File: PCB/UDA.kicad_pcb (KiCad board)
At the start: 2 copper layers, 48 x 48 mm, 36 parts, among them P1 CONN_01X05, U1 MCU-ATMEGA328P-AU(TQFP32), U2 MIC5205-3.3YM5

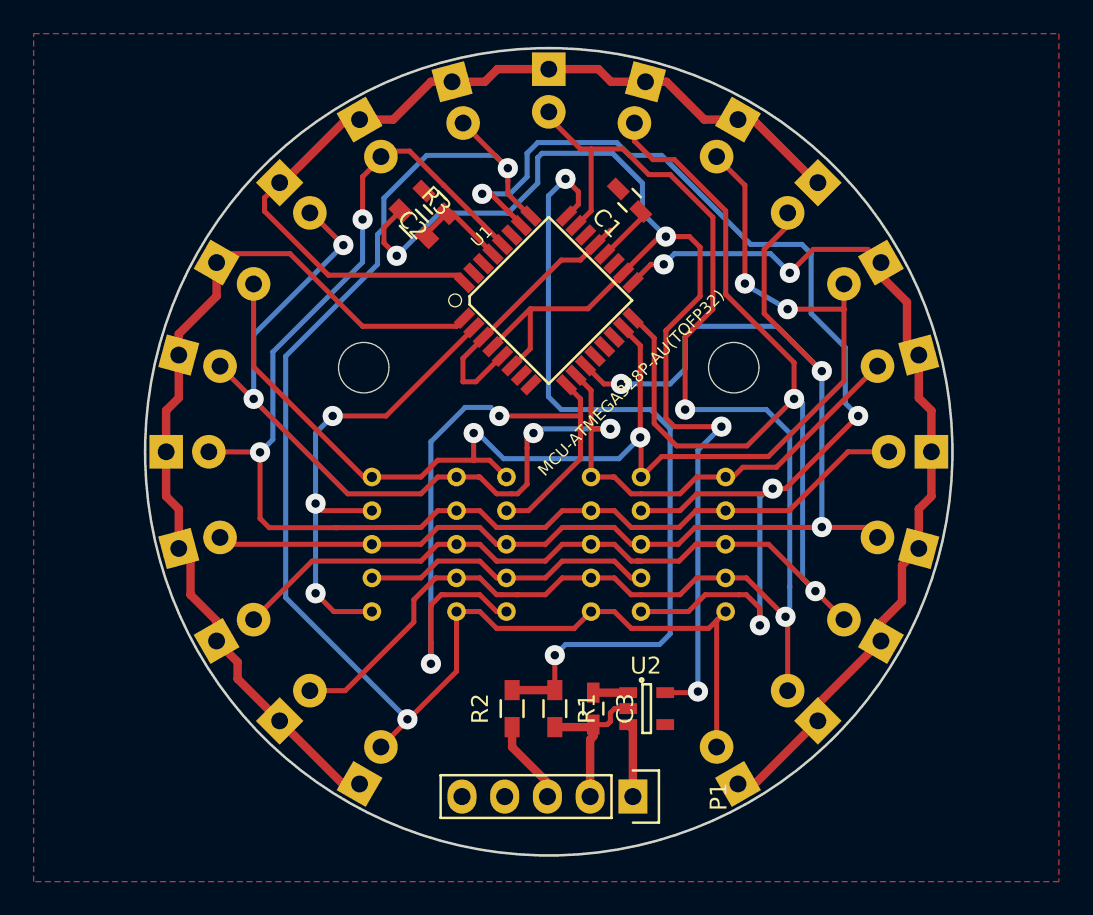
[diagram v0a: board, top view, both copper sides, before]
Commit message: - version finale restante a router
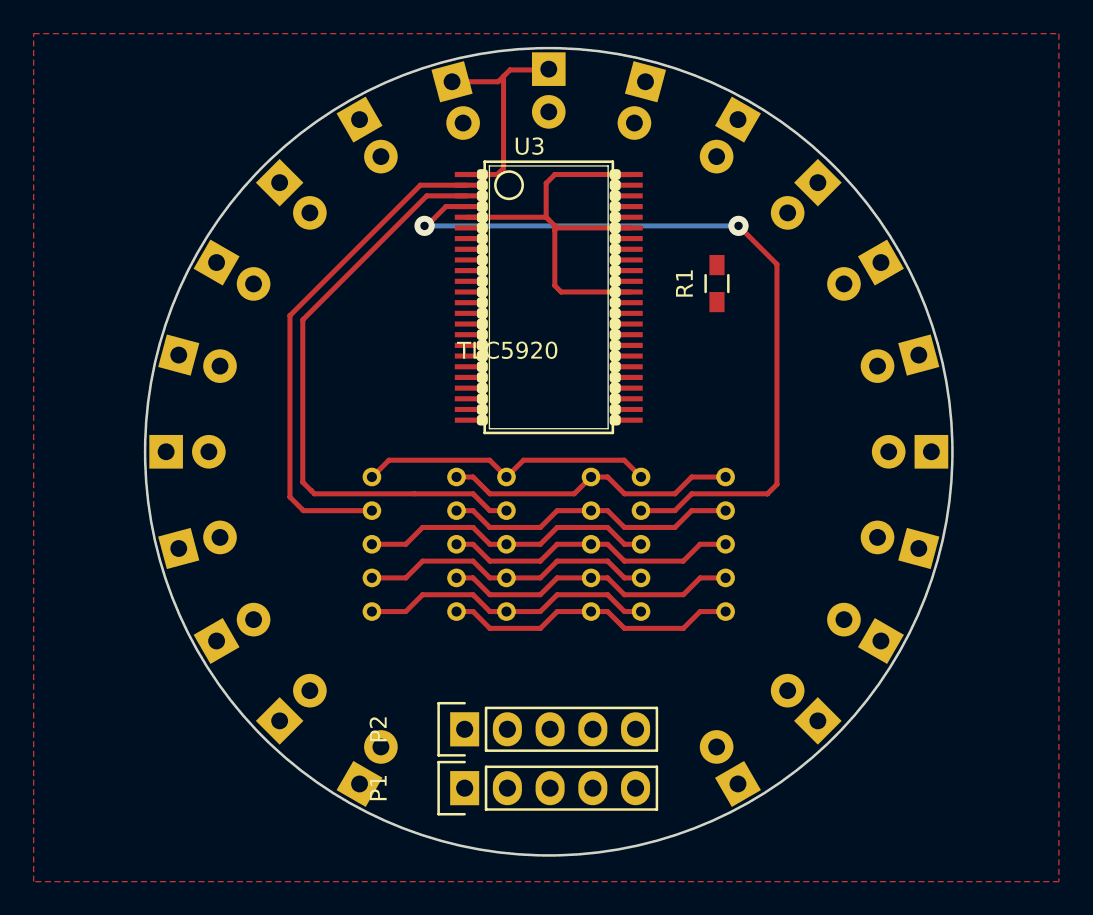
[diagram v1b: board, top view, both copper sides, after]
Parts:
- removed ? (x2): , Perçages:Trou_3mm
- removed C1, C2, C3: 0.1uF, condensateurs:C_0603_HandSoldering
- removed G***: LOGO, Logo:logo
- removed R2: 0.0, resistances:R_0603_HandSoldering
- removed R3: 10k, resistances:R_0603_HandSoldering
- removed U1: MCU-ATMEGA328P-AU(TQFP32), atmel:TQFP32-0.8-7X7MM
- removed U2: MIC5205-3.3YM5, resgulateurs:SOT-23-5
- added P2: CONN_01X05, Barrettes:Pin_Header_Straight_1x05, F.Cu at (81.0, 137.5)
- added U3: TLC5920, Drivers_Afficheurs:SSOP48DL, F.Cu at (86.0, 111.5)
- moved R1 27.0 mm to (96.0, 111.0), turned to 90 degrees
- moved P1 10.0 mm to (81.0, 141.0), turned to 90 degrees
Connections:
- D1 pad 1: COM4 -> COM3
- D1 pad 2: F -> S0
- D10 pad 1: COM5 -> COM3
- D10 pad 2: D -> S9
- D11 pad 1: COM5 -> COM3
- D11 pad 2: E -> S10
- D12 pad 1: COM5 -> COM4
- D12 pad 2: G -> S0
- D13 pad 1: COM5 -> COM4
- D13 pad 2: B -> S1
- D14 pad 1: COM6 -> COM4
- D14 pad 2: B -> S3
- D15 pad 1: COM5 -> COM4
- D15 pad 2: C -> S2
- D16 pad 1: COM6 -> COM4
- D16 pad 2: A -> S4
- D17 pad 1: COM6 -> COM4
- D17 pad 2: F -> S5
- D18 pad 1: COM6 -> COM4
- D18 pad 2: C -> S6
- D19 pad 1: COM6 -> COM4
- D19 pad 2: G -> S7
- D2 pad 1: COM4 -> COM3
- D2 pad 2: B -> S1
- D20 pad 1: COM6 -> COM4
- D20 pad 2: E -> S8
- D21 pad 1: COM6 -> COM4
- D21 pad 2: D -> S9
- D3 pad 1: COM4 -> COM3
- D3 pad 2: G -> S2
- D4 pad 1: COM4 -> COM3
- D4 pad 2: E -> S3
- D5 pad 1: COM4 -> COM3
- D5 pad 2: D -> S4
- D6 pad 1: COM4 -> COM3
- D6 pad 2: A -> S5
- D7 pad 1: COM4 -> COM3
- D7 pad 2: C -> S6
- D8 pad 1: COM5 -> COM3
- D8 pad 2: A -> S7
- D9 pad 1: COM5 -> COM3
- D9 pad 2: F -> S8
- LED1 pad 1: A -> S0
- LED1 pad 10: B -> S1
- LED1 pad 2: F -> S5
- LED1 pad 3: G -> S6
- LED1 pad 4: E -> S4
- LED1 pad 5: D -> S3
- LED1 pad 6: COM1 -> COM5
- LED1 pad 7: DP -> S7
- LED1 pad 8: C -> S2
- LED1 pad 9: COM1 -> COM0
- LED2 pad 1: A -> S0
- LED2 pad 10: B -> S1
- LED2 pad 2: F -> S5
- LED2 pad 3: G -> S6
- LED2 pad 4: E -> S4
- LED2 pad 5: D -> S3
- LED2 pad 6: COM2 -> COM5
- LED2 pad 7: DP -> S7
- LED2 pad 8: C -> S2
- LED2 pad 9: COM2 -> COM1
- LED3 pad 1: A -> S0
- LED3 pad 10: B -> S1
- LED3 pad 2: F -> S5
- LED3 pad 3: G -> S6
- LED3 pad 4: E -> S4
- LED3 pad 5: D -> S3
- LED3 pad 6: COM3 -> COM5
- LED3 pad 7: DP -> S7
- LED3 pad 8: C -> S2
- LED3 pad 9: COM3 -> COM2
- P1 pad 1: +9V -> (no net)
- P1 pad 2: GND -> (no net)
- P1 pad 3: VIN -> (no net)
- P1 pad 4: COM_TX -> (no net)
- P1 pad 5: RX -> (no net)
- R1 pad 1: VAna -> GND
- R1 pad 2: GND -> Net-(R1-Pad2)
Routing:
- net G: track 92.5 -> 0.00 mm, vias 2 -> 0
- net D: track 88.5 -> 0.00 mm, vias 2 -> 0
- net E: track 86.4 -> 0.00 mm, vias 2 -> 0
- net C: track 81.4 -> 0.00 mm, vias 3 -> 0
- net B: track 80.3 -> 0.00 mm, vias 4 -> 0
- net F: track 78.5 -> 0.00 mm, vias 2 -> 0
- net +5V: track 78.0 -> 0.00 mm, vias 4 -> 0
- net A: track 73.3 -> 0.00 mm, vias 4 -> 0
- net COM4: track 54.5 -> 0.00 mm
- net COM6: track 54.4 -> 0.00 mm, vias 2 -> 0
- net VAna: track 48.4 -> 0.00 mm, vias 2 -> 0
- net COM0: track 0.00 -> 46.7 mm, vias 0 -> 2
- net COM1: track 71.3 -> 35.3 mm, vias 4 -> 0
- net COM5: track 53.3 -> 17.7 mm
- net S0: track 0.00 -> 17.7 mm
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
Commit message: - routage casiement fini
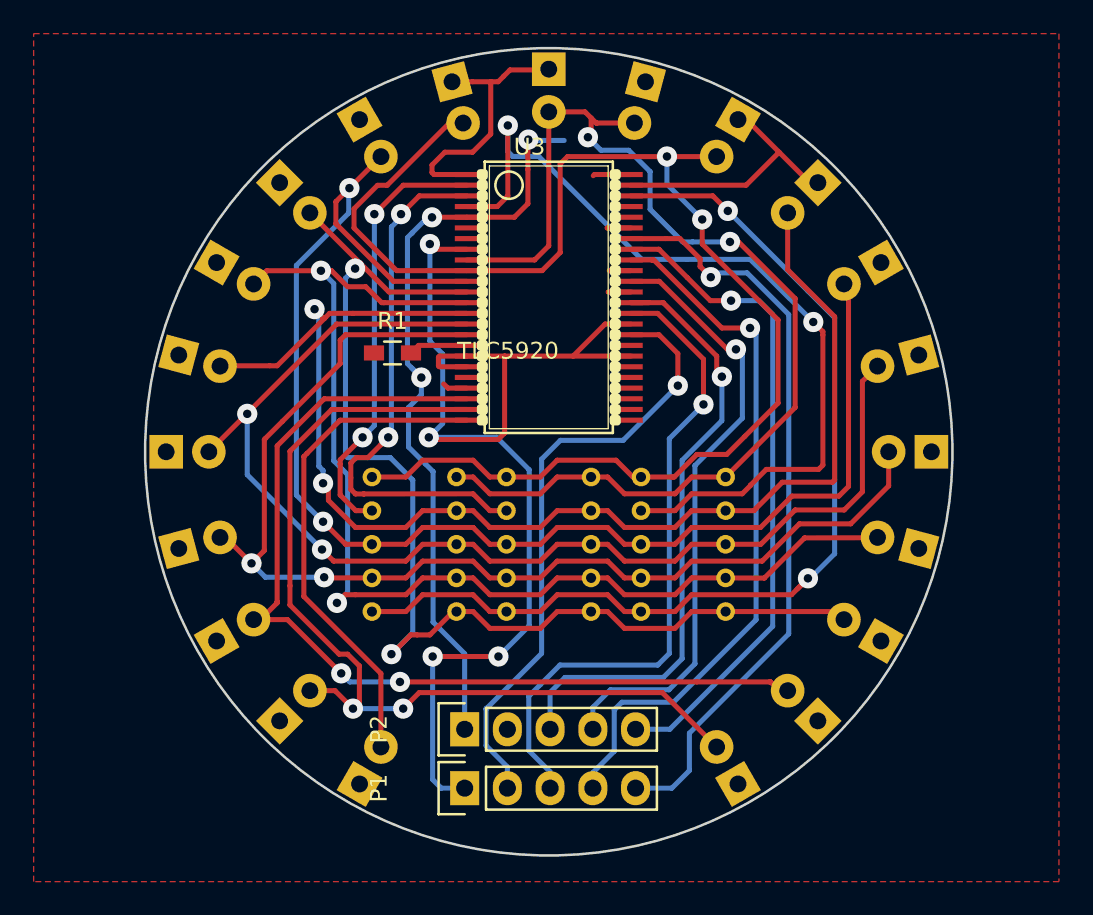
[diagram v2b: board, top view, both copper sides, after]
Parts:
- moved R1 19.7 mm to (76.7, 115.1), turned to 0 degrees
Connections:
- D1 pad 2: S0 -> S6
- D10 pad 2: S9 -> S1
- D11 pad 2: S10 -> S0
- D14 pad 2: S3 -> S2
- D15 pad 2: S2 -> S5
- D16 pad 2: S4 -> S6
- D17 pad 2: S5 -> S7
- D18 pad 2: S6 -> S4
- D19 pad 2: S7 -> S3
- D2 pad 2: S1 -> S4
- D3 pad 2: S2 -> S8
- D4 pad 2: S3 -> S9
- D5 pad 2: S4 -> S10
- D7 pad 2: S6 -> S7
- D8 pad 2: S7 -> S3
- D9 pad 2: S8 -> S2
- P1 pad 1: (no net) -> +5V
- P1 pad 2: (no net) -> DSEL
- P1 pad 3: (no net) -> CSEL2
- P1 pad 4: (no net) -> SCLK
- P1 pad 5: (no net) -> SIN
- P2 pad 1: (no net) -> GND
- P2 pad 3: (no net) -> CSEL1
- P2 pad 4: (no net) -> CSEL0
- P2 pad 5: (no net) -> LATCH
- U3 pad 33: (no net) -> DSEL
- U3 pad 35: (no net) -> CSEL2
- U3 pad 36: (no net) -> CSEL1
- U3 pad 38: (no net) -> CSEL0
- U3 pad 40: (no net) -> SCLK
- U3 pad 41: (no net) -> LATCH
- U3 pad 42: (no net) -> SIN
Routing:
- net +5V: track 0.00 -> 73.6 mm, vias 0 -> 4
- net S1: track 17.7 -> 83.9 mm, vias 0 -> 2
- net S2: track 17.7 -> 83.1 mm, vias 0 -> 2
- net S5: track 17.7 -> 79.4 mm, vias 0 -> 2
- net S8: track 0.00 -> 57.2 mm, vias 0 -> 2
- net S9: track 0.00 -> 55.4 mm, vias 0 -> 2
- net S6: track 17.7 -> 72.1 mm, vias 0 -> 2
- net S4: track 17.7 -> 69.9 mm, vias 0 -> 2
- net S7: track 17.7 -> 69.8 mm, vias 0 -> 2
- net S3: track 17.7 -> 68.4 mm, vias 0 -> 2
- net S0: track 17.7 -> 67.4 mm, vias 0 -> 2
- net SIN: track 0.00 -> 44.9 mm, vias 0 -> 1
- net COM5: track 17.7 -> 60.6 mm, vias 0 -> 2
- net SCLK: track 0.00 -> 42.5 mm, vias 0 -> 1
- net LATCH: track 0.00 -> 39.3 mm, vias 0 -> 1
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
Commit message: - creation du module en 3D pour future utilisation
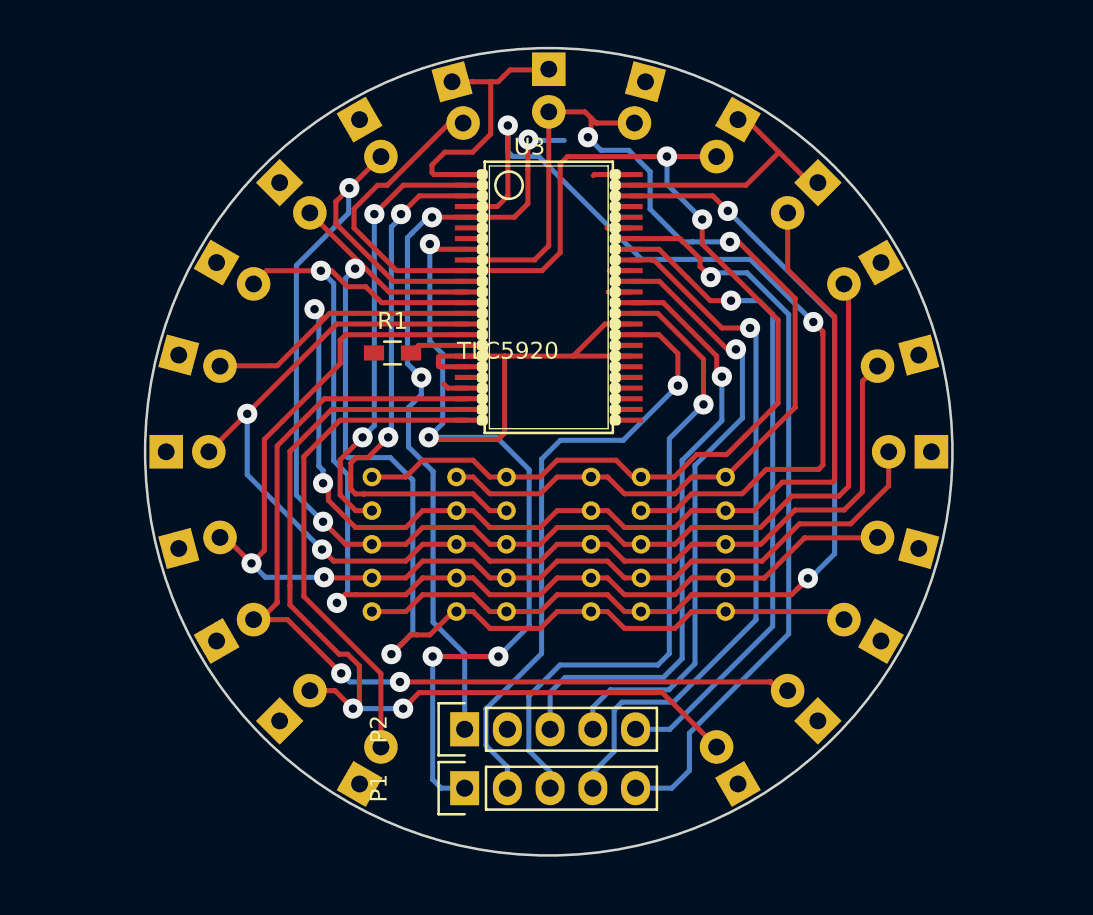
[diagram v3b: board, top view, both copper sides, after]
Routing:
- removed copper zone on F.Cu, net GND

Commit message: - fin du routage
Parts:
- added G***: LOGO, Logo:logo, B.Cu at (84.8, 114.2)
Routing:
- net COM3: track 16.9 -> 73.7 mm
- net COM4: track 15.9 -> 68.4 mm
- net GND: track 55.4 -> 82.5 mm, vias 3 -> 4
- net S1: track 83.9 -> 87.9 mm
- net COM5: track 60.6 -> 61.9 mm

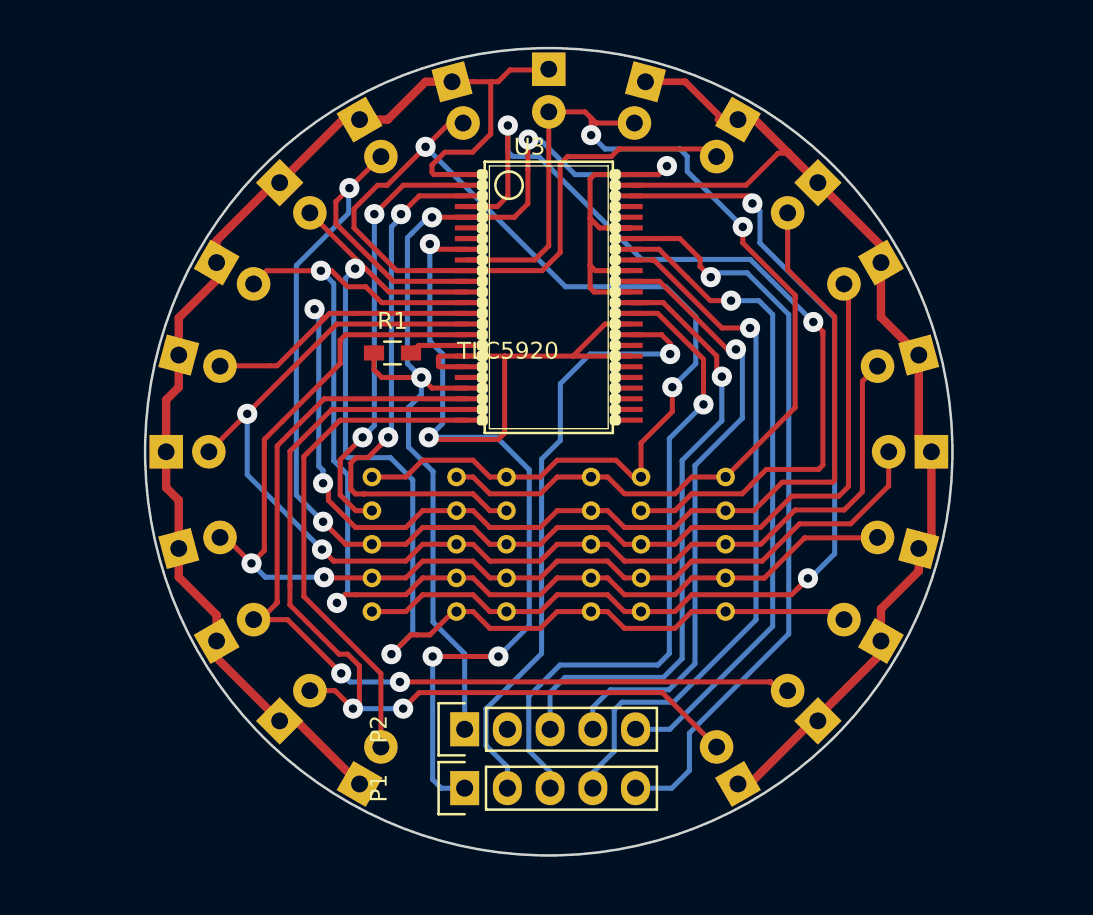
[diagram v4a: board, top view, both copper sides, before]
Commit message: - Correction sur le point des afficheurs 7 segments
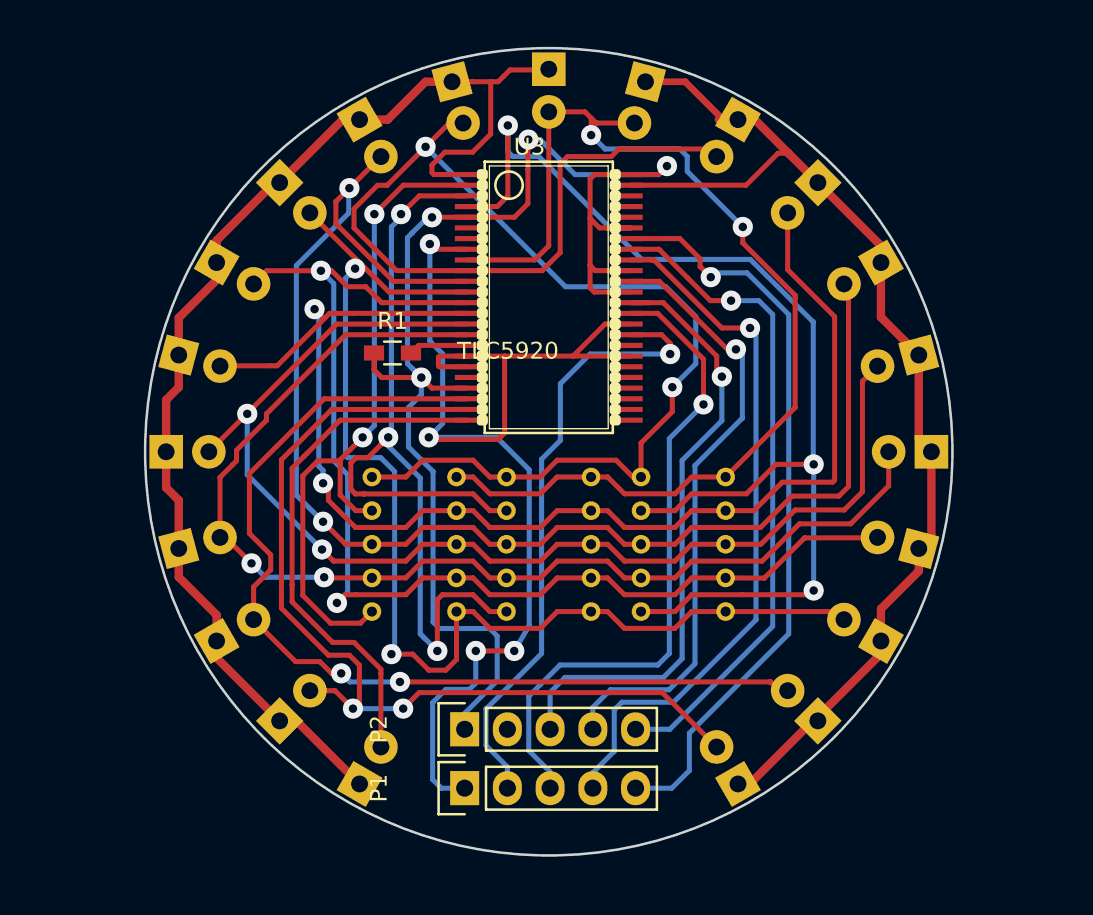
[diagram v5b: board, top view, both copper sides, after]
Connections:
- LED1 pad 6: COM5 -> COM0
- LED2 pad 6: COM5 -> COM1
- LED3 pad 6: COM5 -> COM2
- U3 pad 46: COM5 -> (no net)
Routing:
- net COM5: track 61.9 -> 0.00 mm, vias 2 -> 0
- net COM1: track 32.2 -> 53.8 mm, vias 2 -> 3
- net COM0: track 51.5 -> 69.5 mm, vias 2 -> 3
- net COM2: track 26.0 -> 40.8 mm
- net GND: track 82.5 -> 85.9 mm
- net S3: track 68.4 -> 69.8 mm
- net S10: track 29.8 -> 31.1 mm
- net S9: track 55.4 -> 56.2 mm
- net S7: track 69.8 -> 69.1 mm
- net S8: track 57.2 -> 58.0 mm
